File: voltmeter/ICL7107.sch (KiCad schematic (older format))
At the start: 37 parts, among them J1 +9...12V DC, J2 DP conn., J3 meas. conn, M1 M2.2, M2 M2.2, M3 M2.2, M4 M2.2, U1 LM285Z-1.2, U2 ICL7107, U3 L7805

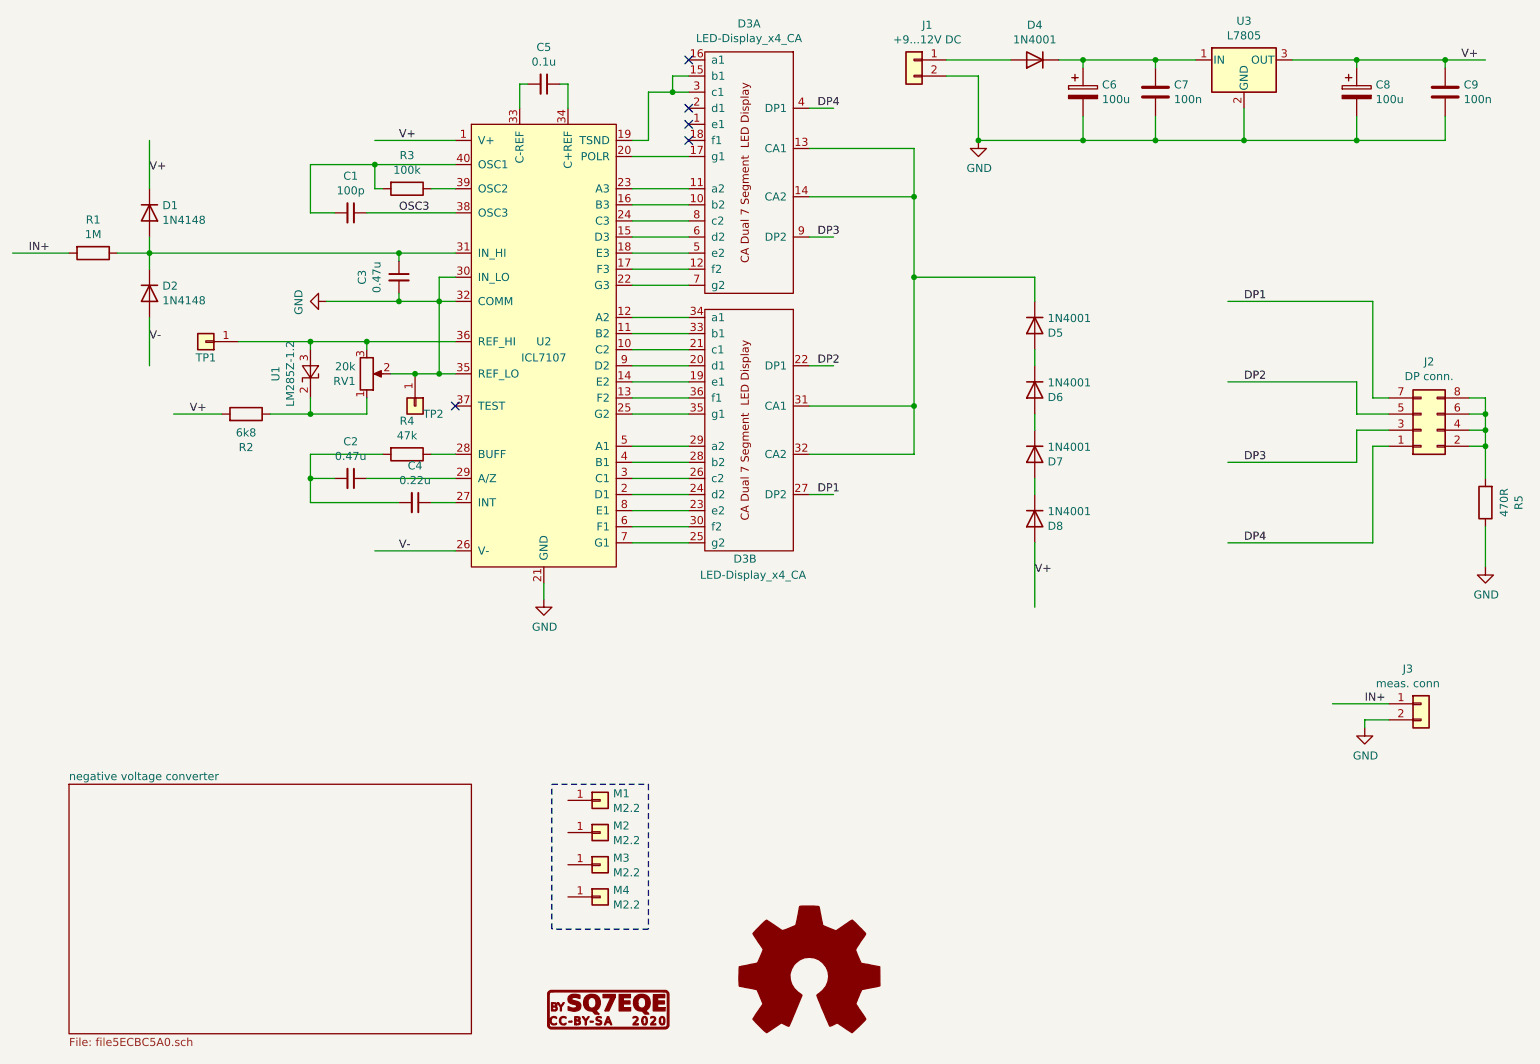
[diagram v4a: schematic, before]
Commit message: update
I have regenerated Gerber files
I make correction of schematic diagram
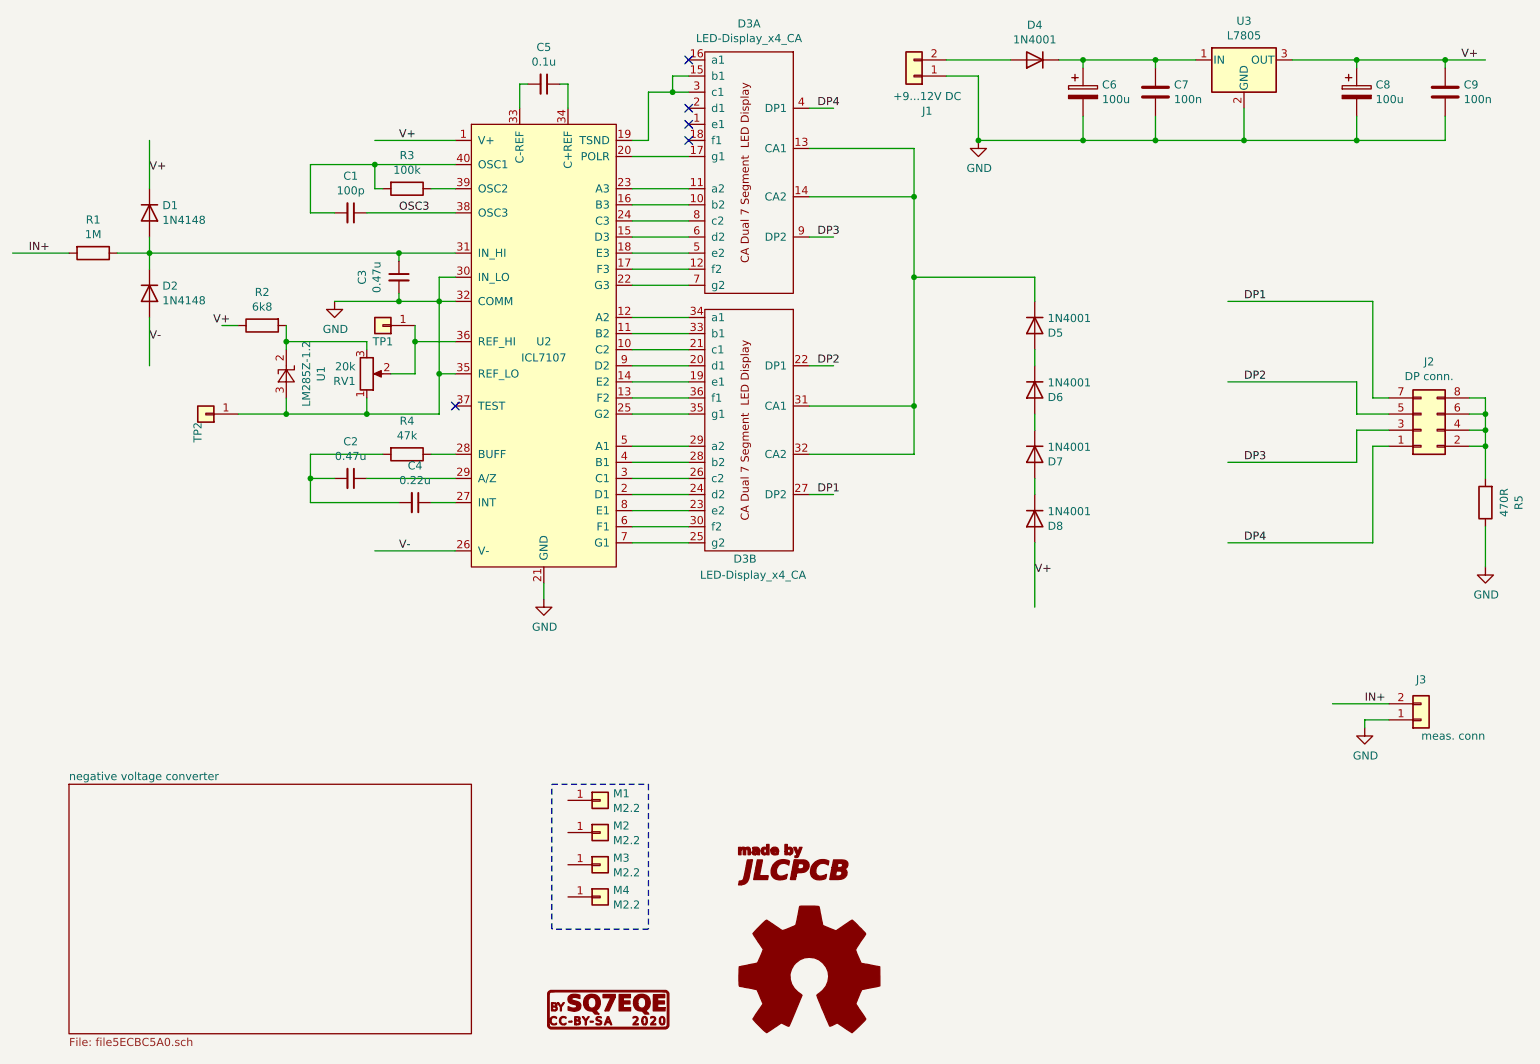
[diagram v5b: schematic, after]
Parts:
- added G2: JLCPCB, logo-sq7eqe:jlcpcb, symbol logo-sq7eqe:JLCPCB
- J1, J3: footprint TerminalBlock:TerminalBlock_Altech_AK300-2_P5.00mm -> Connector_PinHeader_2.54mm:PinHeader_1x02_P2.54mm_Horizontal
- TP1, TP2: footprint Connector_Pin:Pin_D1.0mm_L10.0mm -> Connector_Pin:Pin_D1.3mm_L11.0mm
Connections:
- wire segments 145 -> 148
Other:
- moved on the sheet: R2, TP1, TP2, U1
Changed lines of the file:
@@
 Sheet 1 2
 Title "Digital Voltmeter Module ICL7107"
-Date "2020-07-05"
-Rev "1.5"
+Date "2020-07-31"
+Rev "2.0"
 Comp "MSc. Paweł Sobótka"
 Comment1 "CC-BY-SA 4.0"
@@
 	3550 3000 3550 2950
 Connection ~ 3800 3000
-$Comp
-L Device:R R2
-U 1 1 5ECD43B4
-P 2600 3700
-F 0 "R2" V 2393 3700 50  0000 C CNN
-F 1 "6k8" V 2484 3700 50  0000 C CNN
-F 2 "Resistor_THT:R_Axial_DIN0204_L3.6mm_D1.6mm_P7.62mm_Horizontal" V 2530 3700 50  0001 C CNN
-F 3 "~" H 2600 3700 50  0001 C CNN
-	1    2600 3700
-	0    1    -1   0
-$EndComp
 $Comp
 L Device:R_POT RV1
@@
 	3900 3450 3800 3450
 Wire Wire Line
-	3900 3250 3350 3250
-Wire Wire Line
-	3000 3250 3000 3300
-Wire Wire Line
 	3350 3300 3350 3250
-Connection ~ 3350 3250
-Wire Wire Line
-	3350 3250 3000 3250
 Wire Wire Line
 	3350 3600 3350 3700
-Wire Wire Line
-	3350 3700 3000 3700
-Wire Wire Line
-	3000 3700 3000 3600
-Wire Wire Line
-	2750 3700 3000 3700
-Connection ~ 3000 3700
 Text Label 3550 2450 0    50   ~ 0
 OSC3
@@
 L Connector_Generic:Conn_01x02 J1
 U 1 1 5ECD1D0E
-P 6750 1500
-F 0 "J1" H 6668 1717 50  0000 C CNN
-F 1 "+9...12V DC" H 6668 1626 50  0000 C CNN
-F 2 "TerminalBlock:TerminalBlock_Altech_AK300-2_P5.00mm" H 6750 1500 50  0001 C CNN
-F 3 "~" H 6750 1500 50  0001 C CNN
-	1    6750 1500
-	-1   0    0    -1
+P 6750 1600
+F 0 "J1" H 6668 1817 50  0000 C CNN
+F 1 "+9...12V DC" H 6668 1726 50  0000 C CNN
+F 2 "Connector_PinHeader_2.54mm:PinHeader_1x02_P2.54mm_Horizontal" H 6750 1600 50  0001 C CNN
+F 3 "~" H 6750 1600 50  0001 C CNN
+	1    6750 1600
+	-1   0    0    1
 $EndComp
 Wire Wire Line
@@
 Wire Wire Line
 	4450 4850 4450 4750
-Wire Wire Line
-	2450 3700 2150 3700
-Text Label 2250 3700 0    50   ~ 0
+Text Label 2500 3150 2    50   ~ 0
 V+
 Wire Wire Line
@@
 Wire Wire Line
 	3800 3000 3800 3450
-Connection ~ 3800 3450
-Wire Wire Line
-	3800 3450 3650 3450
 $Comp
 L ICL71xx:ICL7107 U2
@@
 L Connector_Generic:Conn_01x02 J3
 U 1 1 5ECD2461
-P 9900 5500
-F 0 "J3" H 9818 5717 50  0000 C CNN
-F 1 "meas. conn" H 9818 5626 50  0000 C CNN
-F 2 "TerminalBlock:TerminalBlock_Altech_AK300-2_P5.00mm" H 9900 5500 50  0001 C CNN
-F 3 "~" H 9900 5500 50  0001 C CNN
-	1    9900 5500
-	1    0    0    -1
+P 9900 5600
+F 0 "J3" H 9900 5350 50  0000 C CNN
+F 1 "meas. conn" H 10100 5700 50  0000 C CNN
+F 2 "Connector_PinHeader_2.54mm:PinHeader_1x02_P2.54mm_Horizontal" H 9900 5600 50  0001 C CNN
+F 3 "~" H 9900 5600 50  0001 C CNN
+	1    9900 5600
+	1    0    0    1
 $EndComp
 $Comp
@@
 Text Label 8800 4500 0    50   ~ 0
 DP4
-Wire Wire Line
-	9700 5500 9350 5500
 Text Label 9550 5500 0    50   ~ 0
 IN+
@@
 L Connector_Generic:Conn_01x01 TP2
 U 1 1 5ECCF309
-P 3650 3650
-F 0 "TP2" V 3700 3700 50  0000 L CNN
-F 1 "~" V 3613 3730 50  0000 L CNN
-F 2 "Connector_Pin:Pin_D1.0mm_L10.0mm" H 3650 3650 50  0001 C CNN
-F 3 "~" H 3650 3650 50  0001 C CNN
-	1    3650 3650
-	0    1    1    0
-$EndComp
-Connection ~ 3650 3450
-Wire Wire Line
-	3650 3450 3500 3450
+P 2350 3700
+F 0 "TP2" V 2400 3750 50  0000 L CNN
+F 1 "~" V 2313 3780 50  0000 L CNN
+F 2 "Connector_Pin:Pin_D1.3mm_L11.0mm" H 2350 3700 50  0001 C CNN
+F 3 "~" H 2350 3700 50  0001 C CNN
+	1    2350 3700
+	-1   0    0    1
+$EndComp
 $Comp
 L Connector_Generic:Conn_01x01 TP1
 U 1 1 5ECCFF8E
-P 2350 3250
-F 0 "TP1" H 2350 3350 50  0000 C CNN
-F 1 "~" H 2268 3116 50  0000 C CNN
-F 2 "Connector_Pin:Pin_D1.0mm_L10.0mm" H 2350 3250 50  0001 C CNN
-F 3 "~" H 2350 3250 50  0001 C CNN
-	1    2350 3250
+P 3450 3150
+F 0 "TP1" H 3450 3250 50  0000 C CNN
+F 1 "~" H 3368 3016 50  0000 C CNN
+F 2 "Connector_Pin:Pin_D1.3mm_L11.0mm" H 3450 3150 50  0001 C CNN
+F 3 "~" H 3450 3150 50  0001 C CNN
+	1    3450 3150
 	-1   0    0    1
 $EndComp
-Connection ~ 3000 3250
 $Comp
 L Reference_Voltage:LM285Z-1.2 U1
 U 1 1 5ECD40DA
-P 3000 3450
-F 0 "U1" H 3000 3666 50  0000 C CNN
-F 1 "LM285Z-1.2" H 3000 3575 50  0000 C CNN
-F 2 "Package_TO_SOT_THT:TO-92_Inline" H 3000 3250 50  0001 C CIN
-F 3 "http://www.onsemi.com/pub_link/Collateral/LM285-D.PDF" H 3000 3450 50  0001 C CIN
-	1    3000 3450
-	0    -1   1    0
-$EndComp
-Wire Wire Line
-	2550 3250 3000 3250
+P 2850 3450
+F 0 "U1" H 2850 3666 50  0000 C CNN
+F 1 "LM285Z-1.2" H 2850 3575 50  0000 C CNN
+F 2 "Package_TO_SOT_THT:TO-92_Inline" H 2850 3250 50  0001 C CIN
+F 3 "http://www.onsemi.com/pub_link/Collateral/LM285-D.PDF" H 2850 3450 50  0001 C CIN
+	1    2850 3450
+	0    1    -1   0
+$EndComp
 $Comp
 L Graphic:Logo_Open_Hardware_Large LOGO1
@@
 L power:GND #PWR01
 U 1 1 5F042084
-P 3100 3000
-F 0 "#PWR01" H 3100 2750 50  0001 C CNN
-F 1 "GND" H 3105 2827 50  0000 C CNN
-F 2 "" H 3100 3000 50  0001 C CNN
-F 3 "" H 3100 3000 50  0001 C CNN
-	1    3100 3000
-	0    1    1    0
-$EndComp
-Wire Wire Line
-	3550 3000 3100 3000
-Connection ~ 3550 3000
+P 3150 3000
+F 0 "#PWR01" H 3150 2750 50  0001 C CNN
+F 1 "GND" H 3155 2827 50  0000 C CNN
+F 2 "" H 3150 3000 50  0001 C CNN
+F 3 "" H 3150 3000 50  0001 C CNN
+	1    3150 3000
+	1    0    0    -1
+$EndComp
 Wire Wire Line
 	1500 2700 1150 2700
@@
 $EndComp
 Wire Wire Line
-	9700 5600 9550 5600
-Wire Wire Line
 	9550 5600 9550 5650
 Text Label 2000 2200 0    50   ~ 0
@@
 Text Label 2000 3250 0    50   ~ 0
 V-
+Wire Wire Line
+	3800 3450 3800 3700
+Wire Wire Line
+	3800 3700 3350 3700
+Connection ~ 3800 3450
+Connection ~ 3350 3700
+Wire Wire Line
+	3500 3450 3650 3450
+Wire Wire Line
+	3650 3450 3650 3250
+Wire Wire Line
+	3650 3250 3900 3250
+Wire Wire Line
+	2550 3150 2450 3150
+Wire Wire Line
+	2550 3700 2850 3700
+Wire Wire Line
+	2850 3300 2850 3250
+Wire Wire Line
+	2850 3250 3350 3250
+Wire Wire Line
+	2850 3600 2850 3700
+Connection ~ 2850 3700
+Wire Wire Line
+	2850 3700 3350 3700
+Wire Wire Line
+	9350 5500 9700 5500
+Wire Wire Line
+	9550 5600 9700 5600
+$Comp
+L logo-sq7eqe:JLCPCB G2
+U 1 1 5F247858
+P 6000 6500
+F 0 "G2" H 6000 6375 60  0001 C CNN
+F 1 "JLCPCB" H 6000 6625 60  0001 C CNN
+F 2 "logo-sq7eqe:jlcpcb" H 6000 6500 50  0001 C CNN
+F 3 "" H 6000 6500 50  0001 C CNN
+	1    6000 6500
+	1    0    0    -1
+$EndComp
+Connection ~ 3550 3000
+Wire Wire Line
+	3150 3000 3550 3000
+Wire Wire Line
+	3650 3150 3650 3250
+Connection ~ 3650 3250
+$Comp
+L Device:R R2
+U 1 1 5ECD43B4
+P 2700 3150
+F 0 "R2" V 2493 3150 50  0000 C CNN
+F 1 "6k8" V 2584 3150 50  0000 C CNN
+F 2 "Resistor_THT:R_Axial_DIN0204_L3.6mm_D1.6mm_P7.62mm_Horizontal" V 2630 3150 50  0001 C CNN
+F 3 "~" H 2700 3150 50  0001 C CNN
+	1    2700 3150
+	0    -1   1    0
+$EndComp
+Wire Wire Line
+	2850 3150 2850 3250
+Connection ~ 2850 3250
 $EndSCHEMATC

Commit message: upload modified file
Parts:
- U3: footprint Package_TO_SOT_THT:TO-92_Inline -> Package_TO_SOT_THT:TO-220-3_Vertical
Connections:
- net labels added: +5V, -5V
- net labels removed: V+, V-
- wire segments 148 -> 151
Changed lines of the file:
@@
 	3750 2300 3900 2300
 Wire Wire Line
-	3350 2450 3900 2450
+	3350 2450 3700 2450
 $Comp
 L Device:C_Small C5
@@
 Wire Wire Line
 	3900 4550 3400 4550
-Text Label 3550 4550 0    50   ~ 0
-V-
-Text Label 3550 2000 0    50   ~ 0
-V+
 $Comp
 L Regulator_Linear:L7805 U3
@@
 F 0 "U3" H 8800 1742 50  0000 C CNN
 F 1 "L7805" H 8800 1651 50  0000 C CNN
-F 2 "Package_TO_SOT_THT:TO-92_Inline" H 8825 1350 50  0001 L CIN
+F 2 "Package_TO_SOT_THT:TO-220-3_Vertical" H 8825 1350 50  0001 L CIN
 F 3 "http://www.st.com/content/ccc/resource/technical/document/datasheet/41/4f/b3/b0/12/d4/47/88/CD00000444.pdf/files/CD00000444.pdf/jcr:content/translations/en.CD00000444.pdf" H 8800 1450 50  0001 C CNN
 	1    8800 1500
@@
 	10050 1500 10300 1500
 Connection ~ 10050 1500
-Text Label 10150 1500 0    50   ~ 0
-V+
 $Comp
 L Connector_Generic:Conn_01x02 J1
@@
 Wire Wire Line
 	4450 4850 4450 4750
-Text Label 2500 3150 2    50   ~ 0
-V+
 Wire Wire Line
 	5000 4500 5350 4500
@@
 Wire Wire Line
 	7500 4500 7500 4900
-Text Label 7500 4700 0    50   ~ 0
-V+
 Wire Wire Line
 	5350 1700 5250 1700
@@
 Wire Wire Line
 	9550 5600 9550 5650
-Text Label 2000 2200 0    50   ~ 0
-V+
-Text Label 2000 3250 0    50   ~ 0
-V-
 Wire Wire Line
 	3800 3450 3800 3700
@@
 	2850 3150 2850 3250
 Connection ~ 2850 3250
+Text GLabel 3600 2550 0    50   Output ~ 0
+OSC3
+Wire Wire Line
+	3600 2550 3700 2550
+Wire Wire Line
+	3700 2550 3700 2450
+Connection ~ 3700 2450
+Wire Wire Line
+	3700 2450 3900 2450
+$Comp
+L power:-5V #PWR?
+U 1 1 5F2FB8B9
+P 2000 3400
+F 0 "#PWR?" H 2000 3500 50  0001 C CNN
+F 1 "-5V" H 2015 3573 50  0000 C CNN
+F 2 "" H 2000 3400 50  0001 C CNN
+F 3 "" H 2000 3400 50  0001 C CNN
+	1    2000 3400
+	-1   0    0    1
+$EndComp
+$Comp
+L power:-5V #PWR?
+U 1 1 5F2FBD08
+P 3400 4550
+F 0 "#PWR?" H 3400 4650 50  0001 C CNN
+F 1 "-5V" V 3415 4678 50  0000 L CNN
+F 2 "" H 3400 4550 50  0001 C CNN
+F 3 "" H 3400 4550 50  0001 C CNN
+	1    3400 4550
+	0    -1   -1   0
+$EndComp
+$Comp
+L power:+5V #PWR?
+U 1 1 5F2FC6FD
+P 2000 2000
+F 0 "#PWR?" H 2000 1850 50  0001 C CNN
+F 1 "+5V" H 2015 2173 50  0000 C CNN
+F 2 "" H 2000 2000 50  0001 C CNN
+F 3 "" H 2000 2000 50  0001 C CNN
+	1    2000 2000
+	1    0    0    -1
+$EndComp
+$Comp
+L power:+5V #PWR?
+U 1 1 5F2FCFDB
+P 2450 3150
+F 0 "#PWR?" H 2450 3000 50  0001 C CNN
+F 1 "+5V" V 2465 3278 50  0000 L CNN
+F 2 "" H 2450 3150 50  0001 C CNN
+F 3 "" H 2450 3150 50  0001 C CNN
+	1    2450 3150
+	0    -1   -1   0
+$EndComp
+$Comp
+L power:+5V #PWR?
+U 1 1 5F2FD8C0
+P 3400 2000
+F 0 "#PWR?" H 3400 1850 50  0001 C CNN
+F 1 "+5V" V 3415 2128 50  0000 L CNN
+F 2 "" H 3400 2000 50  0001 C CNN
+F 3 "" H 3400 2000 50  0001 C CNN
+	1    3400 2000
+	0    -1   -1   0
+$EndComp
+$Comp
+L power:+5V #PWR?
+U 1 1 5F2FF53F
+P 10300 1500
+F 0 "#PWR?" H 10300 1350 50  0001 C CNN
+F 1 "+5V" H 10315 1673 50  0000 C CNN
+F 2 "" H 10300 1500 50  0001 C CNN
+F 3 "" H 10300 1500 50  0001 C CNN
+	1    10300 1500
+	1    0    0    -1
+$EndComp
+$Comp
+L power:+5V #PWR?
+U 1 1 5F301FA0
+P 7500 4900
+F 0 "#PWR?" H 7500 4750 50  0001 C CNN
+F 1 "+5V" H 7515 5073 50  0000 C CNN
+F 2 "" H 7500 4900 50  0001 C CNN
+F 3 "" H 7500 4900 50  0001 C CNN
+	1    7500 4900
+	-1   0    0    1
+$EndComp
 $EndSCHEMATC
